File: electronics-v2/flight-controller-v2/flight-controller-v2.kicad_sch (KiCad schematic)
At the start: 4 parts

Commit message: fixes in routing
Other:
- sheet power ports: added SENSOR_I2C_SCL, SENSOR_I2C_SDA; removed INT_I2C_SCL, INT_I2C_SDA
- sheet sensors ports: added SENSOR_I2C_SCL, SENSOR_I2C_SDA; removed INT_I2C_SCL, INT_I2C_SDA, VLX_INT, VLX_SCL, VLX_SDA, VLX_XSHUT
- sheet ucontroller ports: added none; removed EXT_I2C3_SCL, EXT_I2C3_SDA, VLX_INT, VLX_XSHUT

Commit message: generate schematic
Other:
- title: (none) -> UAV TVC Goose Flight Controller
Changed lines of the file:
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@@
 (kicad_sch (version 20211123) (generator eeschema)
   (paper "A4")
+  (title_block
+    (title "UAV TVC Goose Flight Controller")
+    (date "2023-07-31")
+    (rev "V2.0")
+  )
   (junction (at 172.72 101.6) (diameter 0) (color 0 0 0 0)
   )

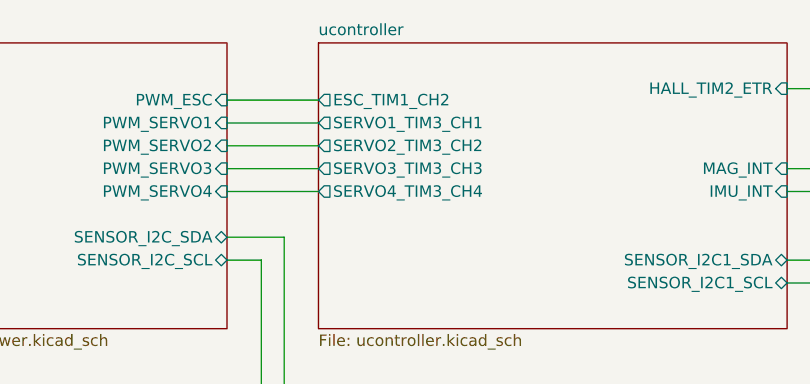
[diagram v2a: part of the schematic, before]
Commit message: fix route name, remove ADC code
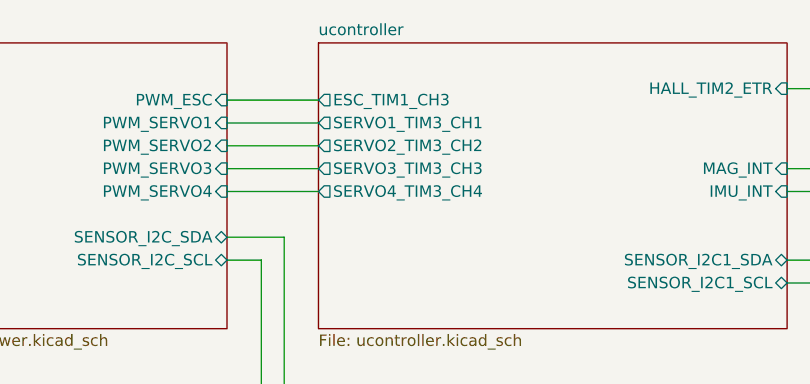
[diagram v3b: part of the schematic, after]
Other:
- sheet ucontroller ports: added ESC_TIM1_CH3; removed ESC_TIM1_CH2
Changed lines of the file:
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@@
       (effects (font (size 1.27 1.27)) (justify right))
-    )
-    (pin "ESC_TIM1_CH2" output (at 114.3 81.28 180)
-      (effects (font (size 1.27 1.27)) (justify left))
     )
     (pin "SERVO3_TIM3_CH3" output (at 114.3 88.9 180)
@@
       (effects (font (size 1.27 1.27)) (justify right))
     )
+    (pin "ESC_TIM1_CH3" output (at 114.3 81.28 180)
+      (effects (font (size 1.27 1.27)) (justify left))
+    )
   )
